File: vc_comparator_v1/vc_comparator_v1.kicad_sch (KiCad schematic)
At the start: 67 parts, among them J1 Conn_02x05_Odd_Even, J2 SIGNAL, J3 OUT, J4 LEVEL, J5 OUT_INV, U1 LM393, U2 LM358, U3 LM358, U4 LM358

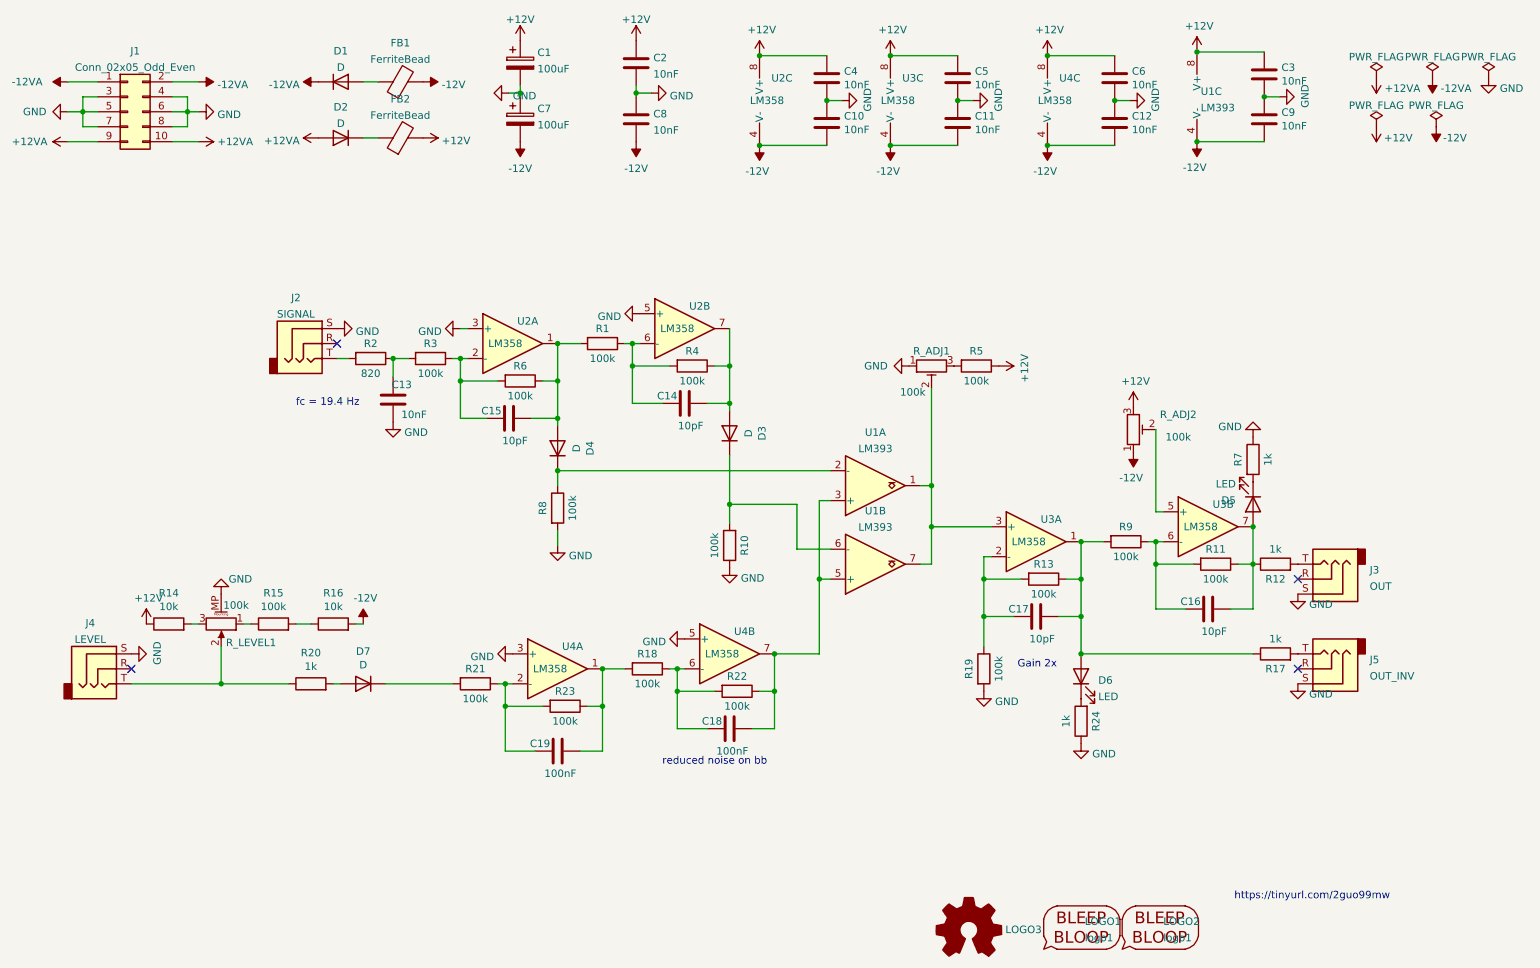
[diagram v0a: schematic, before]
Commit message: Geographic re-annotate and cleanup
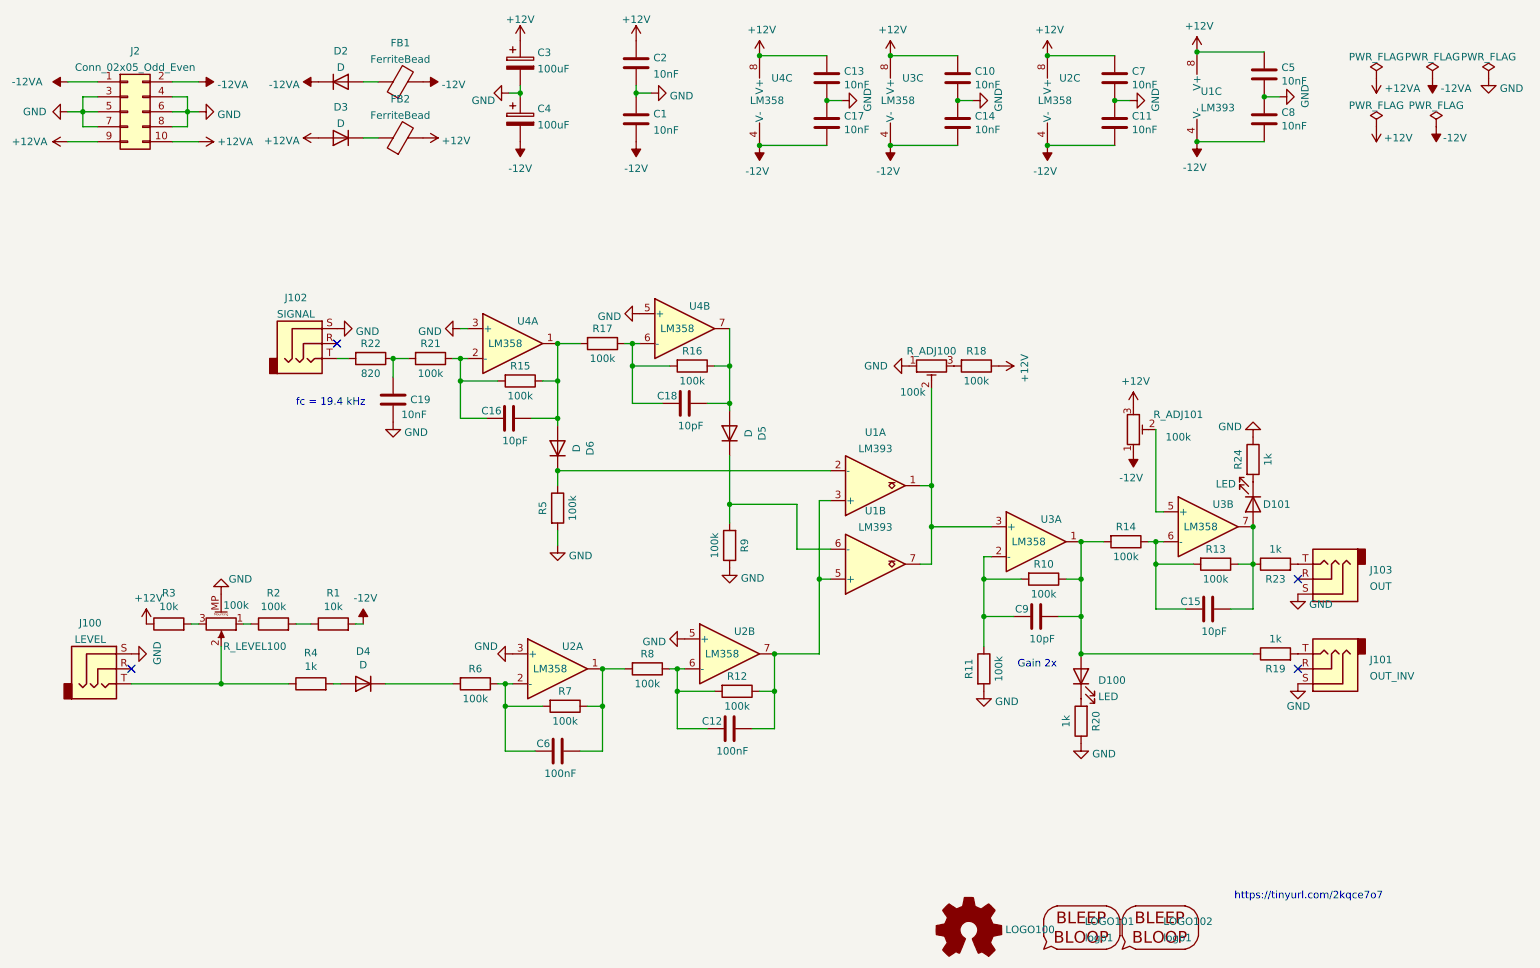
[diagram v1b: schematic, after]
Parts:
- renumbered C8 to C1, C5 to C10, C12 to C11, C18 to C12, C4 to C13, C11 to C14, C16 to C15, C15 to C16, C10 to C17, C14 to C18, C13 to C19, C1 to C3, C7 to C4, C3 to C5, C19 to C6, C6 to C7, C9 to C8, C17 to C9, D6 to D100, D5 to D101, D1 to D2, D2 to D3, D7 to D4, D3 to D5, D4 to D6, J4 to J100, J5 to J101, J2 to J102, J3 to J103, J1 to J2, LOGO3 to LOGO100, LOGO1 to LOGO101, LOGO2 to LOGO102, R16 to R1, R13 to R10, R19 to R11, R22 to R12, R11 to R13, R9 to R14, R6 to R15, R4 to R16, R1 to R17, R5 to R18, R17 to R19, R15 to R2, R24 to R20, R3 to R21, R2 to R22, R12 to R23, R7 to R24, R14 to R3, R20 to R4, R8 to R5, R21 to R6, R23 to R7, R18 to R8, R10 to R9, R_ADJ1 to R_ADJ100, R_ADJ2 to R_ADJ101, R_LEVEL1 to R_LEVEL100, U4 to U2, U2 to U4
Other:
- note added: "fc = 19.4 kHz"
- note added: "https://tinyurl.com/2kqce7o7"
- note removed: "fc = 19.4 Hz"
- note removed: "https://tinyurl.com/2guo99mw"
- note removed: "reduced noise on bb"
- title: (none) -> VC Comparator
